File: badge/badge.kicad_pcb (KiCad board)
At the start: 2 copper layers, 50 x 50 mm, 59 parts, among them J1 Conn_02x03_Odd_Even, Q1 BSS83P, SW1 SK-3296S-01-L1, SW2 SW_Push, U1 ATtiny424-SSU, U2 MT3608

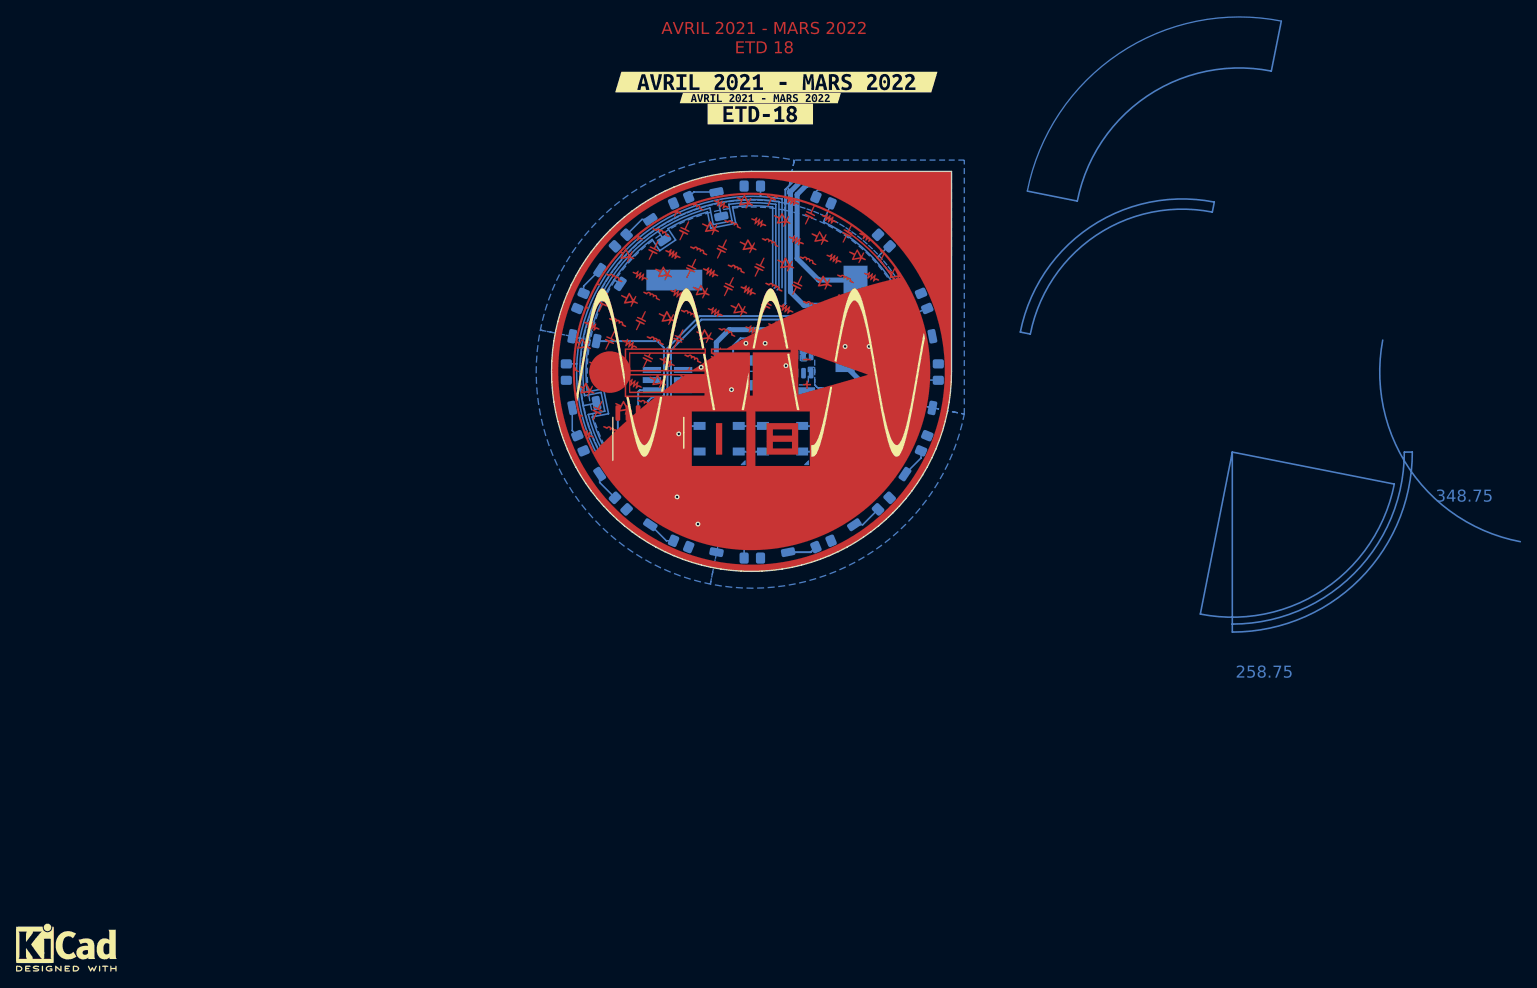
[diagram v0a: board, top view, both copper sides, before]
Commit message: routing finished. need to update one last time the badge's footprint tho
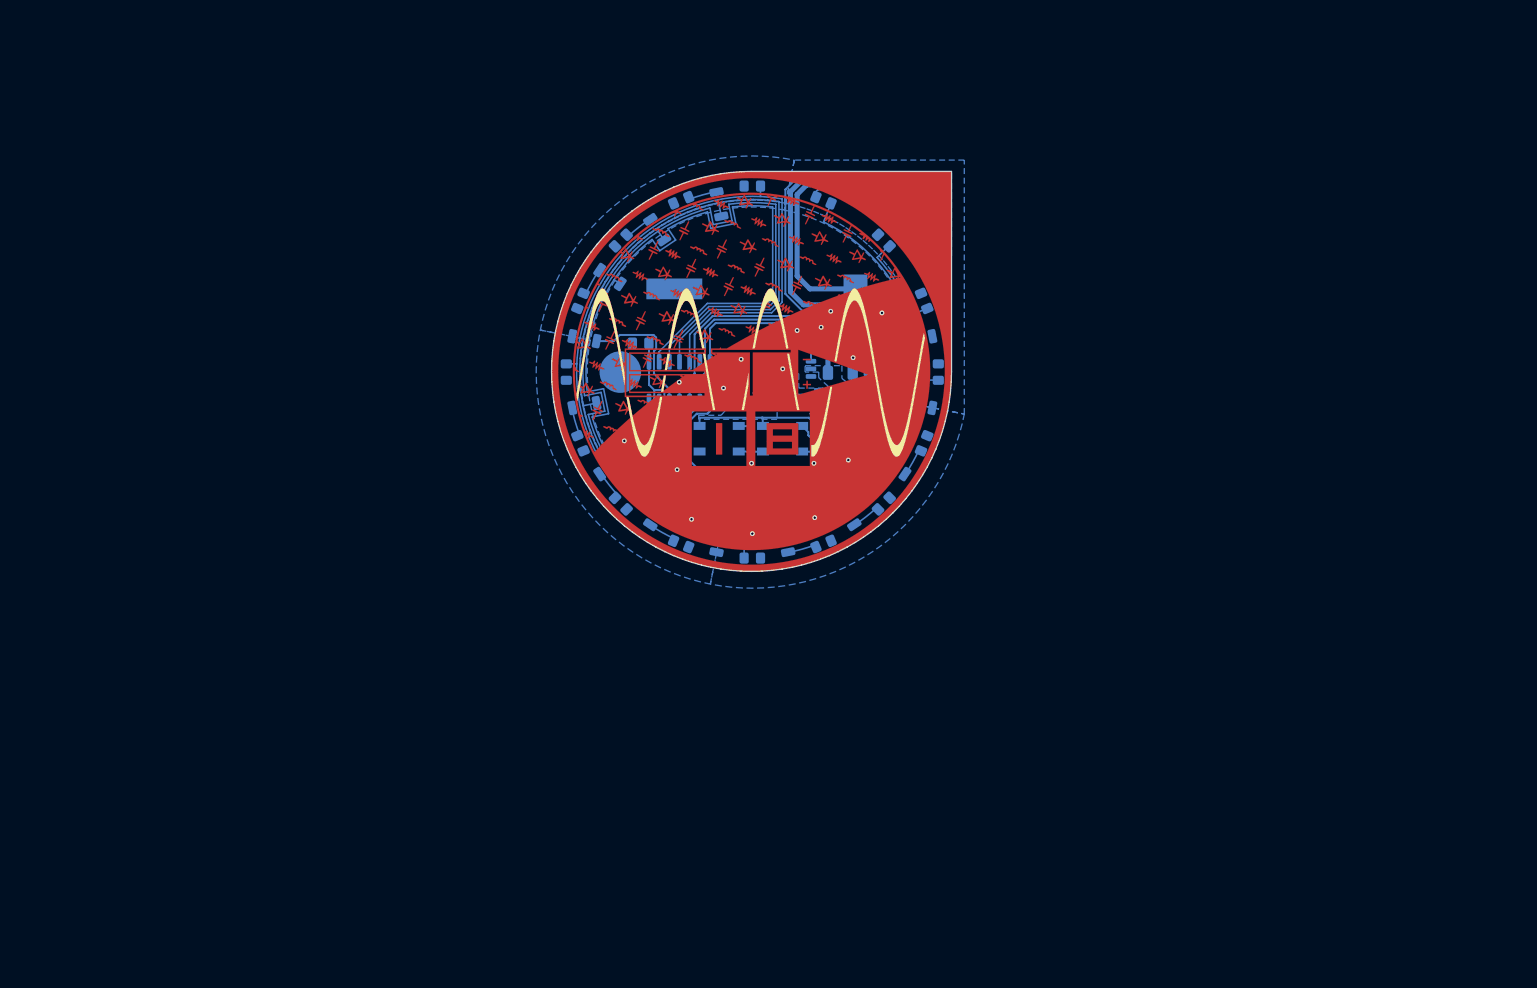
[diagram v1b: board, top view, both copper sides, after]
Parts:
- removed G1: KiCAD LOGO Small, Symbol:KiCad-Logo2_5mm_SilkScreen
- removed kibuzzard-635F9BF9: G***, kibuzzard-635F9BF9
- removed kibuzzard-635F9CA7: G***, kibuzzard-635F9CA7
- removed kibuzzard-635F9CB1: G***, kibuzzard-635F9CB1
- added LOGO1: Logo_Open_Hardware_Small, Symbol:OSHW-Logo2_7.3x6mm_SilkScreen, B.Cu at (-12.5, 12.5)
- added LOGO2: GUIGUR LOGO, guigur-lib:guigur_engineering_extra_small_logo, B.Cu at (15.4, -22.8)
- added LOGO3: KiCAD LOGO Small, guigur-lib:kicad_design_with_7.5mm, B.Cu at (11.0, 13.8)
- added LOGO4: WEEE LOGO, Symbol:WEEE-Logo_4.2x6mm_SilkScreen, B.Cu at (16.5, 6.30)
- added kibuzzard-637A9580: G***, kibuzzard-637A9580, B.Cu at (-15.6, -5.95)
- added kibuzzard-637A9837: G***, kibuzzard-637A9837, B.Cu at (15.4, -20.0)
- added kibuzzard-637A9899: G***, kibuzzard-637A9899, B.Cu at (20.2, -12.6)
- added kibuzzard-637A9AEB: G***, kibuzzard-637A9AEB, B.Cu at (-15.6, -7.40)
- added kibuzzard-637A9DDD: G***, kibuzzard-637A9DDD, B.Cu at (0.00, 19.3)
- C5: footprint Resistor_SMD:R_0805_2012Metric_Pad1.20x1.40mm_HandSolder -> Capacitor_SMD:C_0805_2012Metric_Pad1.18x1.45mm_HandSolder
- H2, U1: moved to B.Cu
- L1: footprint Inductor_SMD:L_6.3x6.3_H3 -> Inductor_SMD:L_Bourns-SRN4018
- moved C1 19.1 mm to (-14.0, -3.60), turned to 180 degrees
- moved U1 7.49 mm to (-9.10, 1.20), turned to -90 degrees
- moved J1 6.55 mm to (-12.0, 7.40), turned to 180 degrees
- moved R10 4.20 mm to (-8.40, 13.4)
- moved C2 3.35 mm to (11.0, 0.10)
- moved L1 2.41 mm to (10.0, 3.80), turned to 180 degrees
- moved C3 1.97 mm to (-1.40, 1.80)
- moved H1 1.30 mm to (16.5, 0.00)
- moved H2 1.30 mm to (-16.5, 0.00), turned to 180 degrees
- moved D17 1.28 mm to (3.60, 3.60)
- moved R9 1.24 mm to (-3.60, -0.40)
- moved BT1 1.10 mm to (0.00, -10.4)
- moved JP17 1.02 mm to (14.0, -5.80)
- moved R6 0.85 mm to (1.80, -1.00)
- moved R5 0.85 mm to (1.80, 0.60)
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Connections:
- J1 pad 1: /UDPI/ROW3 -> /UDPI/ROW0
- R1 pad 1: /ROW0 -> /UDPI/ROW0
- R4 pad 1: /UDPI/ROW3 -> /ROW3
- U1 pad 10: /UDPI/ROW3 -> /UDPI/ROW0
- U1 pad 11: /ROW2 -> /ROW1
- U1 pad 12: /ROW1 -> /ROW2
- U1 pad 13: /ROW0 -> /ROW3
- U1 pad 7: /USR_BUTTON -> /5V_EN
- U1 pad 9: /5V_EN -> /USR_BUTTON
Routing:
- net /ROW0: track 49.6 -> 0.00 mm
- net /UDPI/ROW0: track 0.00 -> 48.3 mm
- net (no net): track 33.0 -> 0.00 mm
- net /ROW3: track 0.00 -> 21.7 mm
- net /COL1: track 127.9 -> 148.9 mm
- net /COL0: track 119.8 -> 138.4 mm
- net /COL3: track 165.0 -> 180.8 mm
- net /5V_EN: track 33.2 -> 22.9 mm
- net /USR_BUTTON: track 29.2 -> 21.7 mm
- net /NEO_SIG: track 42.2 -> 36.0 mm
- net /UDPI/ROW3: track 4.46 -> 0.00 mm
- net /ROW1: track 41.8 -> 38.1 mm
- net /COL2: track 161.9 -> 165.6 mm
- net GND: track 48.9 -> 45.5 mm, vias 11 -> 19
- net +5V: track 23.6 -> 21.2 mm
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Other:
- board text removed: "258.75"
- board text removed: "348.75"
- board text removed: "AVRIL 2021 - MARS 2022 ETD 18"

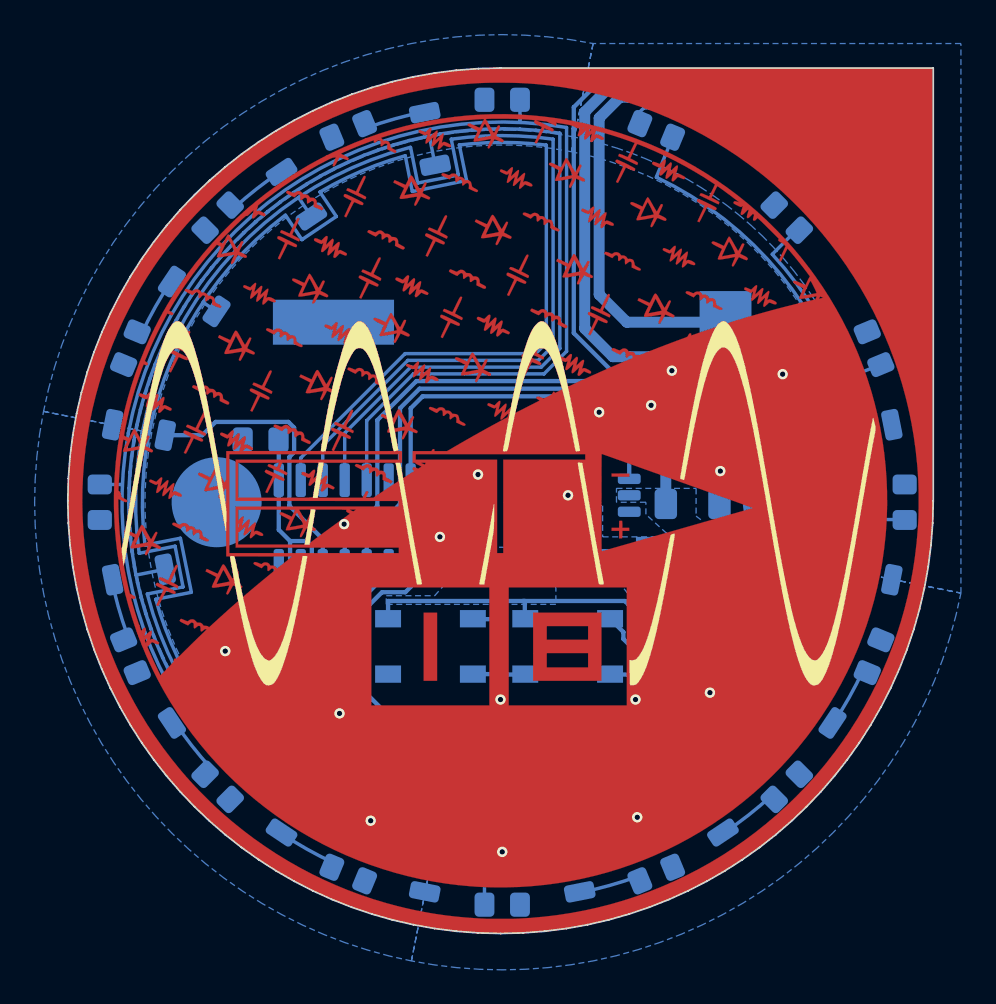
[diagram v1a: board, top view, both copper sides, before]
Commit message: updated the footprint of the badge and corrected the button footprint
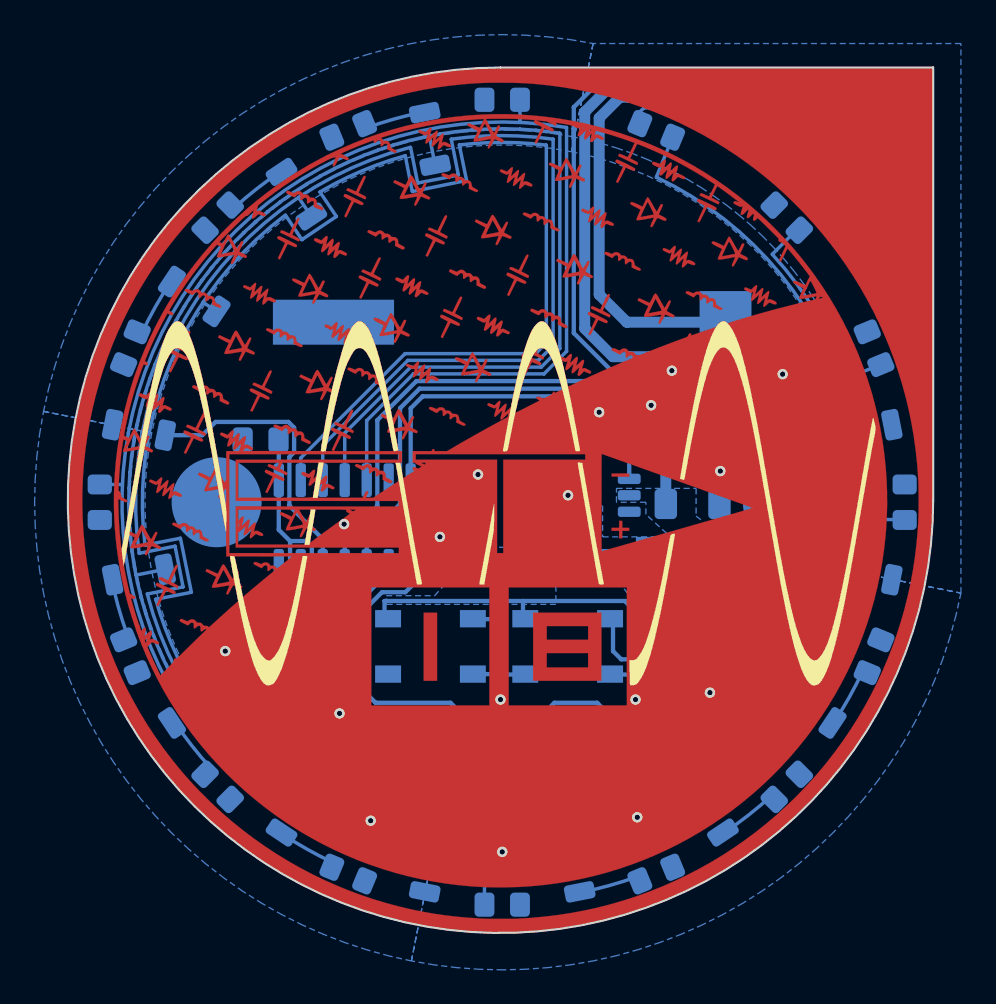
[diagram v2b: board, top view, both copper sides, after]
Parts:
- SW2: footprint Button_Switch_SMD:SW_Push_1P1T_NO_CK_KSC6xxJ -> Button_Switch_SMD:SW_Push_1P1T_NO_6x6mm_H9.5mm
- moved C5 0.60 mm to (-6.20, 14.5)
- moved R10 0.60 mm to (-9.00, 13.4)
- moved kibuzzard-637A9DDD 0.50 mm to (0.00, 18.8)
- moved SW2 0.40 mm to (0.00, 14.8)
- moved kibuzzard-637A9899 0.20 mm to (20.2, -12.8)
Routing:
- net /USR_BUTTON: track 21.7 -> 23.4 mm
- net VCC: track 75.0 -> 73.7 mm
- net /NEO_1: track 7.54 -> 8.30 mm
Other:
- outline, holes or cut-outs redrawn

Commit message: pcb finished and ready to be ordered
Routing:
- net /COL3: track 180.8 -> 176.7 mm
- net /COL2: track 165.6 -> 163.8 mm
- net GND: track 45.5 -> 43.9 mm
- net Net-(JP17-Pad1): track 43.6 -> 42.5 mm
- net /ROW1: track 38.1 -> 37.2 mm
- net /NEO_1: track 8.30 -> 9.23 mm
- net Net-(BT1-Pad1): track 38.6 -> 37.8 mm
- net /NEO_SIG: track 36.5 -> 35.7 mm
- net /ROW3: track 21.7 -> 21.0 mm
- net /UDPI/ROW0: track 48.2 -> 47.6 mm
- net /5V_EN: track 22.9 -> 22.3 mm
- net /COL0: track 138.4 -> 137.8 mm
